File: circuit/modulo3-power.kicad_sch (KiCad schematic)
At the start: 25 parts, among them Q1 IRF4905SPBF, SW1 SW_DPDT, U1 MCP16331, U2 LM1117-5.0

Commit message: fv-1 mostly done; power progressed
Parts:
- added J1, J2, J3, J4: HOLE, myAmp:MountingHole, symbol myAmp:HOLE
- added U3: PWR_CONN, myAmp:PWR_CONN, symbol myAmp:PWR_CONN
- added U4: AMPCTRL, myAmp:AMPCTRL, symbol myAmp:AMPCTRL
- BT1: footprint myAmp:XT60PW-M -> myAmp:XT60-M
- D3: footprint myAmp:LED_D3.0mm_PCBedge -> myAmp:LED_D3.0mm
- R1, R4, R5: footprint myAmp:C_0805 -> myAmp:R_10MM
- R2, R3: footprint myAmp:C_0805 -> myAmp:R_0805
- SW1: value SW_DPDT -> on/off; footprint (none) -> myAmp:SW_DPDT
- U2: footprint myAmp:SOT-223 -> myAmp:TO-252-3
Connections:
- net +5V: now also U3.3 (5V)
- net GND: now also U3.1 (GND), U4.1 (GND)
- net at SW1.1: now also C2.1, Q1.3 (S), R1.2
- net at SW1.2: now also F1.2
- net VDD renamed +BATT
- net +BATT: now also U3.2 (30V)
- no-connect marks 2 -> 5
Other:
- moved on the sheet: BT1, C2, D3, F1, Q1, R1, R4, R5

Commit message: lotsa things :)
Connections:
- net GND: now also SW1.6
- net MUTE: now reaches SW1.5
- net MUTE: now also U4.3 (MUTE)
- no-connect marks 5 -> 6
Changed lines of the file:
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@@
   (junction (at 67.31 26.67) (diameter 0) (color 0 0 0 0)
   )
+  (no_connect (at 45.72 113.03))
   (no_connect (at 45.72 105.41))
   (no_connect (at 46.99 31.75))
@@
     (stroke (width 0) (type default))
   )
+  (wire (pts (xy 34.29 33.02) (xy 41.91 33.02))
+    (stroke (width 0) (type default))
+  )
   (wire (pts (xy 210.82 40.005) (xy 215.9 40.005))
     (stroke (width 0) (type default))
@@
     (stroke (width 0) (type default))
   )
+  (wire (pts (xy 46.99 34.29) (xy 48.26 34.29))
+    (stroke (width 0) (type default))
+  )
   (wire (pts (xy 196.85 90.17) (xy 196.85 95.25))
     (stroke (width 0) (type default))
@@
     (stroke (width 0) (type default))
   )
+  (wire (pts (xy 48.26 34.29) (xy 48.26 35.56))
+    (stroke (width 0) (type default))
+  )
   (wire (pts (xy 183.515 90.17) (xy 187.96 90.17))
     (stroke (width 0) (type default))
@@
     (stroke (width 0) (type default))
   )
+  (wire (pts (xy 45.72 110.49) (xy 48.26 110.49))
+    (stroke (width 0) (type default))
+  )
   (wire (pts (xy 184.15 36.195) (xy 184.15 38.735))
     (stroke (width 0) (type default))
@@
   (wire (pts (xy 237.49 28.575) (xy 237.49 29.845))
     (stroke (width 0) (type default))
+  )
+  (label "MUTE" (at 34.29 33.02 0) (fields_autoplaced)
+    (effects (font (size 1.27 1.27)) (justify left bottom))
+  )
+  (label "MUTE" (at 48.26 110.49 0) (fields_autoplaced)
+    (effects (font (size 1.27 1.27)) (justify left bottom))
   )
   (global_label "6V8" (shape input) (at 183.515 90.17 180) (fields_autoplaced)
@@
         )
       )
+    )
+  )
+  (symbol (lib_id "power:GND") (at 48.26 35.56 0) (unit 1)
+    (in_bom yes) (on_board yes) (dnp no) (fields_autoplaced)
+    (property "Reference" "#PWR02" (at 48.26 41.91 0)
+      (effects (font (size 1.27 1.27)) hide)
+    )
+    (property "Value" "GND" (at 48.26 40.005 0)
+      (effects (font (size 1.27 1.27)))
+    )
+    (property "Footprint" "" (at 48.26 35.56 0)
+      (effects (font (size 1.27 1.27)) hide)
+    )
+    (property "Datasheet" "" (at 48.26 35.56 0)
+      (effects (font (size 1.27 1.27)) hide)
+    )
+    (pin "1")
+    (instances
+      (project "modulo3-power"
+        (path "/e63e39d7-6ac0-4ffd-8aa3-1841a4541b55"
+          (reference "#PWR02") (unit 1)
+        )
+      )

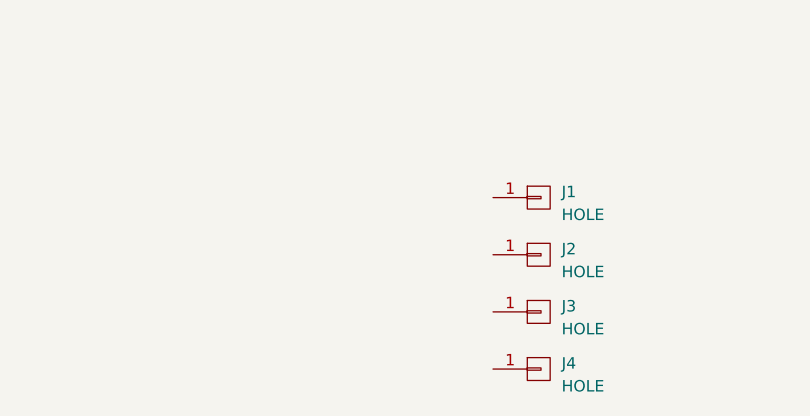
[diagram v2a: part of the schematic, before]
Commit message: tweaked power amp and fv1
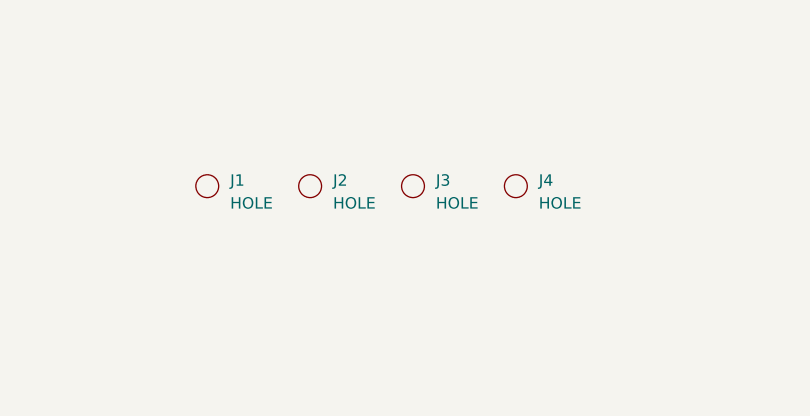
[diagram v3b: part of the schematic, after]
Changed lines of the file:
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@@
+    )
+  )
+  (symbol (lib_name "HOLE_1") (lib_id "myAmp:HOLE") (at 140.97 171.45 0) (unit 1)
+    (in_bom yes) (on_board yes) (dnp no) (fields_autoplaced)
+    (property "Reference" "J2" (at 143.51 170.815 0)
+      (effects (font (size 1.27 1.27)) (justify left))
+    )
+    (property "Value" "HOLE" (at 143.51 173.355 0)
+      (effects (font (size 1.27 1.27)) (justify left))
+    )
+    (property "Footprint" "myAmp:MountingHole" (at 140.97 171.45 0)
+      (effects (font (size 1.27 1.27)) hide)
+    )
+    (property "Datasheet" "" (at 140.97 171.45 0)
+      (effects (font (size 1.27 1.27)) hide)
+    )
+    (instances
+      (project "modulo3-power"
+        (path "/e63e39d7-6ac0-4ffd-8aa3-1841a4541b55"
+          (reference "J2") (unit 1)
+        )
+      )
+    )
+  )
+  (symbol (lib_name "HOLE_1") (lib_id "myAmp:HOLE") (at 152.4 171.45 0) (unit 1)
+    (in_bom yes) (on_board yes) (dnp no) (fields_autoplaced)
+    (property "Reference" "J3" (at 154.94 170.815 0)
+      (effects (font (size 1.27 1.27)) (justify left))
+    )
+    (property "Value" "HOLE" (at 154.94 173.355 0)
+      (effects (font (size 1.27 1.27)) (justify left))
+    )
+    (property "Footprint" "myAmp:MountingHole" (at 152.4 171.45 0)
+      (effects (font (size 1.27 1.27)) hide)
+    )
+    (property "Datasheet" "" (at 152.4 171.45 0)
+      (effects (font (size 1.27 1.27)) hide)
+    )
+    (instances
+      (project "modulo3-power"
+        (path "/e63e39d7-6ac0-4ffd-8aa3-1841a4541b55"
+          (reference "J3") (unit 1)
+        )
+      )
     )
   )
@@
     )
   )
-  (symbol (lib_id "myAmp:HOLE") (at 166.37 185.42 0) (unit 1)
+  (symbol (lib_name "HOLE_1") (lib_id "myAmp:HOLE") (at 129.54 171.45 0) (unit 1)
     (in_bom yes) (on_board yes) (dnp no) (fields_autoplaced)
-    (property "Reference" "J3" (at 168.91 184.785 0)
-      (effects (font (size 1.27 1.27)) (justify left))
-    )
-    (property "Value" "HOLE" (at 168.91 187.325 0)
-      (effects (font (size 1.27 1.27)) (justify left))
-    )
-    (property "Footprint" "myAmp:MountingHole" (at 166.37 185.42 0)
-      (effects (font (size 1.27 1.27)) hide)
-    )
-    (property "Datasheet" "" (at 166.37 185.42 0)
-      (effects (font (size 1.27 1.27)) hide)
-    )
-    (pin "1")
-    (instances
-      (project "modulo3-power"
-        (path "/e63e39d7-6ac0-4ffd-8aa3-1841a4541b55"
-          (reference "J3") (unit 1)
+    (property "Reference" "J1" (at 132.08 170.815 0)
+      (effects (font (size 1.27 1.27)) (justify left))
+    )
+    (property "Value" "HOLE" (at 132.08 173.355 0)
+      (effects (font (size 1.27 1.27)) (justify left))
+    )
+    (property "Footprint" "myAmp:MountingHole" (at 129.54 171.45 0)
+      (effects (font (size 1.27 1.27)) hide)
+    )
+    (property "Datasheet" "" (at 129.54 171.45 0)
+      (effects (font (size 1.27 1.27)) hide)
+    )
+    (instances
+      (project "modulo3-power"
+        (path "/e63e39d7-6ac0-4ffd-8aa3-1841a4541b55"
+          (reference "J1") (unit 1)
         )
       )
@@
     )
   )
+  (symbol (lib_name "HOLE_1") (lib_id "myAmp:HOLE") (at 163.83 171.45 0) (unit 1)
+    (in_bom yes) (on_board yes) (dnp no) (fields_autoplaced)
+    (property "Reference" "J4" (at 166.37 170.815 0)
+      (effects (font (size 1.27 1.27)) (justify left))
+    )
+    (property "Value" "HOLE" (at 166.37 173.355 0)
+      (effects (font (size 1.27 1.27)) (justify left))
+    )
+    (property "Footprint" "myAmp:MountingHole" (at 163.83 171.45 0)
+      (effects (font (size 1.27 1.27)) hide)
+    )
+    (property "Datasheet" "" (at 163.83 171.45 0)
+      (effects (font (size 1.27 1.27)) hide)
+    )
+    (instances
+      (project "modulo3-power"
+        (path "/e63e39d7-6ac0-4ffd-8aa3-1841a4541b55"
+          (reference "J4") (unit 1)
+        )
+      )
+    )
+  )
   (symbol (lib_id "power:GND") (at 187.96 105.41 0) (unit 1)
     (in_bom yes) (on_board yes) (dnp no)
@@
         (path "/e63e39d7-6ac0-4ffd-8aa3-1841a4541b55"
           (reference "#PWR0105") (unit 1)
-        )
-      )
-    )
-  )
-  (symbol (lib_id "myAmp:HOLE") (at 166.37 179.07 0) (unit 1)
-    (in_bom yes) (on_board yes) (dnp no) (fields_autoplaced)
-    (property "Reference" "J2" (at 168.91 178.435 0)
-      (effects (font (size 1.27 1.27)) (justify left))
-    )
-    (property "Value" "HOLE" (at 168.91 180.975 0)
-      (effects (font (size 1.27 1.27)) (justify left))
-    )
-    (property "Footprint" "myAmp:MountingHole" (at 166.37 179.07 0)
-      (effects (font (size 1.27 1.27)) hide)
-    )
-    (property "Datasheet" "" (at 166.37 179.07 0)
-      (effects (font (size 1.27 1.27)) hide)
-    )
-    (pin "1")
-    (instances
-      (project "modulo3-power"
-        (path "/e63e39d7-6ac0-4ffd-8aa3-1841a4541b55"
-          (reference "J2") (unit 1)
         )
       )
@@
     )
   )
-  (symbol (lib_id "myAmp:HOLE") (at 166.37 172.72 0) (unit 1)
-    (in_bom yes) (on_board yes) (dnp no) (fields_autoplaced)
-    (property "Reference" "J1" (at 168.91 172.085 0)
-      (effects (font (size 1.27 1.27)) (justify left))
-    )
-    (property "Value" "HOLE" (at 168.91 174.625 0)
-      (effects (font (size 1.27 1.27)) (justify left))
-    )
-    (property "Footprint" "myAmp:MountingHole" (at 166.37 172.72 0)
-      (effects (font (size 1.27 1.27)) hide)
-    )
-    (property "Datasheet" "" (at 166.37 172.72 0)
-      (effects (font (size 1.27 1.27)) hide)
-    )
-    (pin "1")
-    (instances
-      (project "modulo3-power"
-        (path "/e63e39d7-6ac0-4ffd-8aa3-1841a4541b55"
-          (reference "J1") (unit 1)
-        )
-      )
-    )
-  )
   (symbol (lib_id "myAmp:C") (at 67.31 31.75 0) (unit 1)
     (in_bom yes) (on_board yes) (dnp no)
@@
         )
       )
-    )
-  )
-  (symbol (lib_id "myAmp:HOLE") (at 166.37 191.77 0) (unit 1)
-    (in_bom yes) (on_board yes) (dnp no) (fields_autoplaced)
-    (property "Reference" "J4" (at 168.91 191.135 0)
-      (effects (font (size 1.27 1.27)) (justify left))
-    )
-    (property "Value" "HOLE" (at 168.91 193.675 0)
-      (effects (font (size 1.27 1.27)) (justify left))
-    )
-    (property "Footprint" "myAmp:MountingHole" (at 166.37 191.77 0)
-      (effects (font (size 1.27 1.27)) hide)
-    )
-    (property "Datasheet" "" (at 166.37 191.77 0)
-      (effects (font (size 1.27 1.27)) hide)
-    )
-    (pin "1")
-    (instances
-      (project "modulo3-power"
-        (path "/e63e39d7-6ac0-4ffd-8aa3-1841a4541b55"
-          (reference "J4") (unit 1)
-        )
-      )
